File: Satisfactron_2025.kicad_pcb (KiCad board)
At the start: 2 copper layers, 409.5 x 93 mm, 188 parts, among them J1 USB-TYPE-C-018, J10 GT-BTP30002-0350B-019B, J11 Conn_01x03, J12 LED strip, J2 GT-BTP30002-0350B-019B, J3 TF_PUSH, J4 GT-BTP30002-0350B-019B, J5 PZ254V-11-04P_C2691448, J6 Conn_01x06, J7 GT-BTP30002-0350B-019B, J8 GT-BTP30002-0350B-019B, J9 GT-BTP30002-0350B-019B, Q1 2N7002, SW1 MSK-22D18G4_051, SW10 SPVN310101, SW11 SPVN310101, SW12 SPVN310101, SW13 SPVN310101, SW14 SPVN310101, SW15 SPVN310101, SW16 SPVN310101, SW17 SPVN310101, SW18 SPVN310101, SW19 SPVN310101, SW2 TS-1088-AR02016, SW20 SPVN310101, SW3 SPVN310101, SW4 SPVN310101, SW5 TS-1088-AR02016, SW6 TS-1088-AR02016, SW7 TS-1088-AR02016, SW8 SPVN310101, SW9 SPVN310101, U1 AMS1117-3.3, U10 WS2811C, U11 WS2811C, U12 WS2811C, U13 WS2811C, U14 TSSP77038TT, U2 TPS82130, U3 ESP32-S3-WROOM-1-N16R8, U4 TSSP77038TR, U5 TSSP77038TR, U6 TSSP77038TR, U7 TSSP77038TR, U8 TSSP77038TR, U9 WS2811C, U99 TSSP77038TT

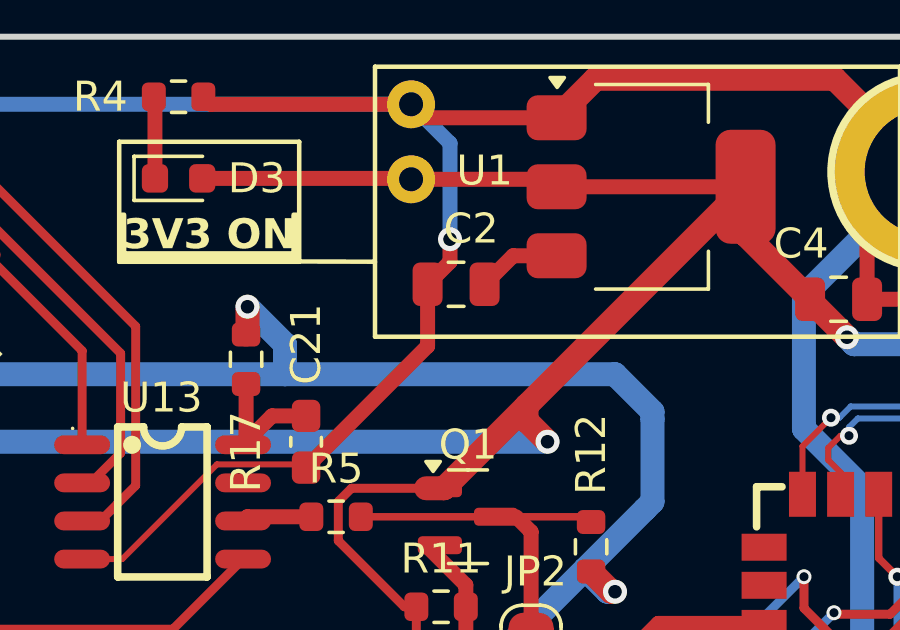
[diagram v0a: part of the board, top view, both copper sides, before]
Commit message: Correct corresponding PCB mistake, 5V connected to 3V3 reg now
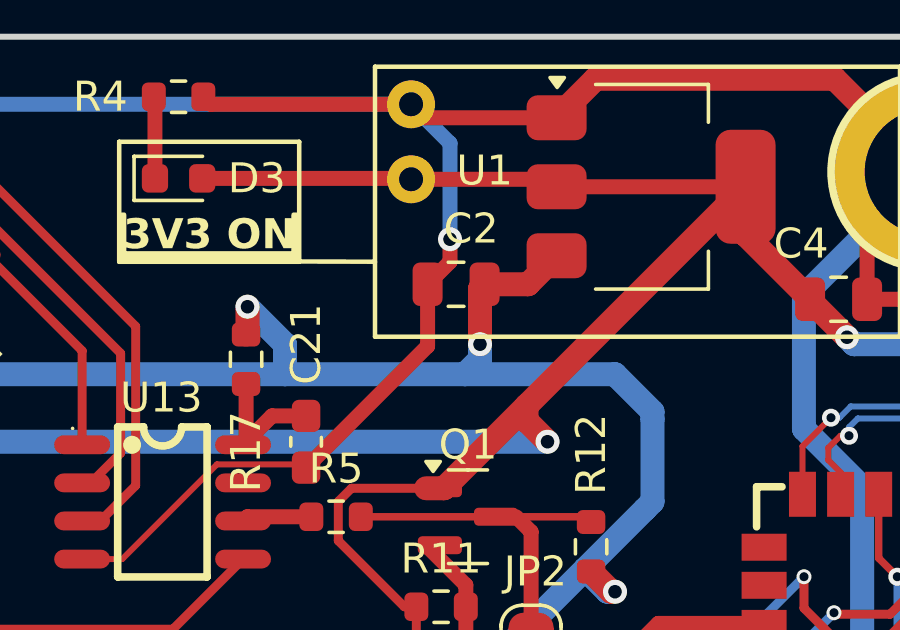
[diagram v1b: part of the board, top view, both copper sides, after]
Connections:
- C2 pad 1: Net-(U1-VI) -> +5L
- U1 pad 3: Net-(U1-VI) -> +5L
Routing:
- net +5L: track 789.1 -> 795.2 mm, vias 11 -> 12
- net Net-(U1-VI): track 2.79 -> 0.00 mm
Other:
- board text added: "h2"
- board text removed: "h1"
